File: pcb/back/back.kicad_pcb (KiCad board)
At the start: 4 copper layers, 26.5 x 26.5 mm, 60 parts, among them J1 Conn_01x02, J2 USB_B_Micro, U1 ATSAMD21G18A-A, U2 LSM6DS3, U3 XC6206PxxxMR, U4 TP4057

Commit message: Update accelerometer
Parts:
- U2: value LSM6DS3 -> LIS3DH; footprint Package_LGA:LGA-14_3x2.5mm_P0.5mm_LayoutBorder3x4y -> Package_LGA:LGA-16_3x3mm_P0.5mm_LayoutBorder3x5y
- moved R19 0.15 mm to (159.0, 91.5), turned to -90 degrees
- moved R18 0.14 mm to (159.0, 89.6)
- moved C5 0.13 mm to (154.0, 89.9)
- moved C6 0.13 mm to (154.0, 90.9)
- turned U2 to 90 degrees
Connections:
- U2 pad 1: GND -> +3V3
- U2 pad 10: unconnected-(U2-NC-Pad10) -> GND
- U2 pad 11: unconnected-(U2-NC-Pad11) -> /AINT
- U2 pad 12: +3V3 -> GND
- U2 pad 13: /SCL -> unconnected-(U2-ADC3-Pad13)
- U2 pad 14: /SDA -> +3V3
- U2 pad 4: /AINT -> /SCL
- U2 pad 5: +3V3 -> GND
- U2 pad 6: GND -> /SDA
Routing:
- net /SWDIO: track 19.5 -> 16.0 mm
- net GND: track 10.4 -> 13.4 mm, vias 29 -> 30
- net +3V3: track 62.5 -> 63.9 mm
- net /AINT: track 11.1 -> 11.7 mm

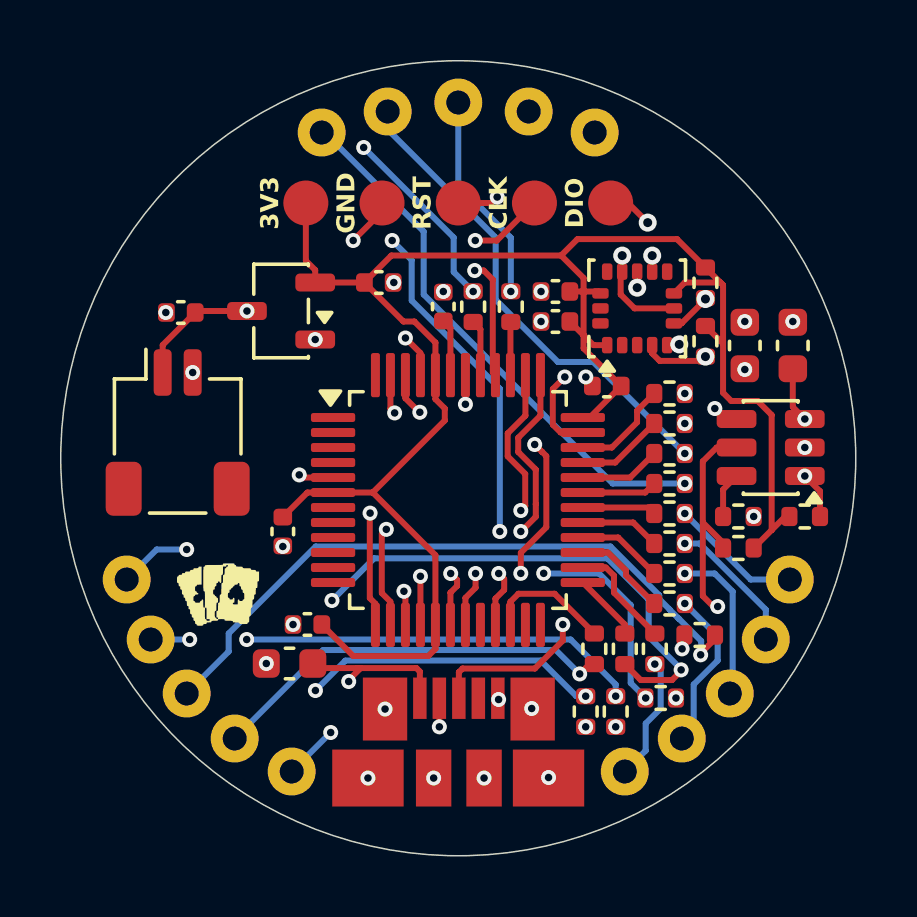
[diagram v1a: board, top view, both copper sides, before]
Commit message: Add tooling holes
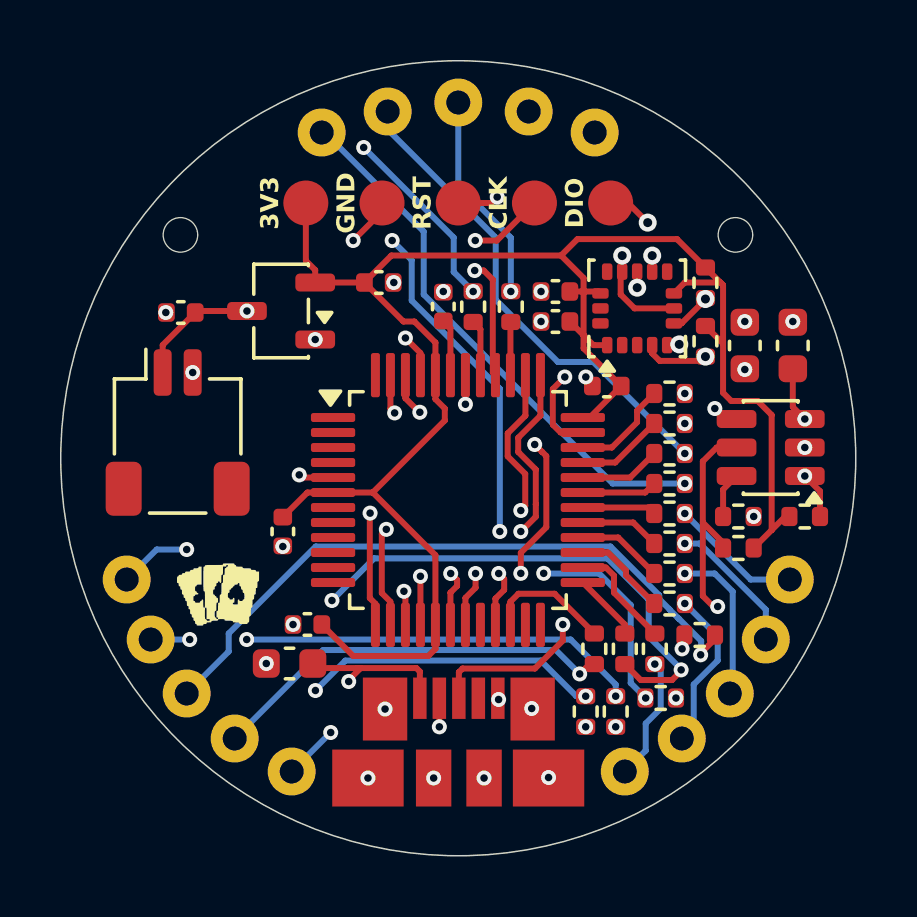
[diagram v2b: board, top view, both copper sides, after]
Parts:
- added REF**: ToolingHole_1.152mm, MountingHole:ToolingHole_1.152mm, F.Cu at (160.0, 88.0)
- added REF**: ToolingHole_1.152mm, MountingHole:ToolingHole_1.152mm, F.Cu at (141.5, 88.0)

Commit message: Format schematics
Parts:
- turned C10 to 0 degrees
- turned C11 to 0 degrees
- turned C3 to 90 degrees
- turned C4 to 90 degrees
- turned C6 to 0 degrees
- turned C8 to 90 degrees
- turned R21 to 180 degrees
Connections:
- C10 pad 1: +3V3 -> GND
- C10 pad 2: GND -> +3V3
- C11 pad 1: VBUS -> GND
- C11 pad 2: GND -> VBUS
- C3 pad 1: GND -> VBUS
- C3 pad 2: VBUS -> GND
- C4 pad 1: GND -> +BATT
- C4 pad 2: +BATT -> GND
- C6 pad 1: +3V3 -> GND
- C6 pad 2: GND -> +3V3
- C8 pad 1: GND -> Net-(U1-VDDCORE)
- C8 pad 2: Net-(U1-VDDCORE) -> GND
- R21 pad 1: Net-(U4-PROG) -> GND
- R21 pad 2: GND -> Net-(U4-PROG)

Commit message: Use 2k I2C resistors
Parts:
- R18, R19: value 10k -> 2k
- turned R18 to 90 degrees
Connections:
- R18 pad 1: +3V3 -> /SDA
- R18 pad 2: /SDA -> +3V3
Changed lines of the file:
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@@
 			)
 		)
-		(property "Value" "10k"
+		(property "Value" "2k"
 			(at 0 1.17 90)
 			(layer "F.Fab")
@@
 	(footprint "Resistor_SMD:R_0402_1005Metric"
 		(layer "F.Cu")
-		(at 159 89.5975 -90)
+		(at 159 89.5975 90)
 		(descr "Resistor SMD 0402 (1005 Metric), square (rectangular) end terminal, IPC-7351 nominal, (Body size source: IPC-SM-782 page 72, https://www.pcb-3d.com/wordpress/wp-content/uploads/ipc-sm-782a_amendment_1_and_2.pdf), generated with kicad-footprint-generator")
 		(tags "resistor")
@@
 			)
 		)
-		(property "Value" "10k"
+		(property "Value" "2k"
 			(at 0 1.17 90)
 			(layer "F.Fab")
@@
 		(duplicate_pad_numbers_are_jumpers no)
 		(fp_line
+			(start -0.153641 -0.38)
+			(end 0.153641 -0.38)
+			(stroke
+				(width 0.12)
+				(type solid)
+			)
+			(layer "F.SilkS")
+		)
+		(fp_line
 			(start -0.153641 0.38)
 			(end 0.153641 0.38)
@@
 		)
 		(fp_line
-			(start -0.153641 -0.38)
-			(end 0.153641 -0.38)
-			(stroke
-				(width 0.12)
-				(type solid)
-			)
-			(layer "F.SilkS")
+			(start 0.93 -0.47)
+			(end 0.93 0.47)
+			(stroke
+				(width 0.05)
+				(type solid)
+			)
+			(layer "F.CrtYd")
+		)
+		(fp_line
+			(start -0.93 -0.47)
+			(end 0.93 -0.47)
+			(stroke
+				(width 0.05)
+				(type solid)
+			)
+			(layer "F.CrtYd")
+		)
+		(fp_line
+			(start 0.93 0.47)
+			(end -0.93 0.47)
+			(stroke
+				(width 0.05)
+				(type solid)
+			)
+			(layer "F.CrtYd")
 		)
 		(fp_line
@@
 		)
 		(fp_line
-			(start 0.93 0.47)
-			(end -0.93 0.47)
-			(stroke
-				(width 0.05)
-				(type solid)
-			)
-			(layer "F.CrtYd")
-		)
-		(fp_line
-			(start -0.93 -0.47)
-			(end 0.93 -0.47)
-			(stroke
-				(width 0.05)
-				(type solid)
-			)
-			(layer "F.CrtYd")
-		)
-		(fp_line
-			(start 0.93 -0.47)
-			(end 0.93 0.47)
-			(stroke
-				(width 0.05)
-				(type solid)
-			)
-			(layer "F.CrtYd")
+			(start 0.525 -0.27)
+			(end 0.525 0.27)
+			(stroke
+				(width 0.1)
+				(type solid)
+			)
+			(layer "F.Fab")
+		)
+		(fp_line
+			(start -0.525 -0.27)
+			(end 0.525 -0.27)
+			(stroke
+				(width 0.1)
+				(type solid)
+			)
+			(layer "F.Fab")
+		)
+		(fp_line
+			(start 0.525 0.27)
+			(end -0.525 0.27)
+			(stroke
+				(width 0.1)
+				(type solid)
+			)
+			(layer "F.Fab")
 		)
 		(fp_line
@@
 			(layer "F.Fab")
 		)
-		(fp_line
-			(start 0.525 0.27)
-			(end -0.525 0.27)
-			(stroke
-				(width 0.1)
-				(type solid)
-			)
-			(layer "F.Fab")
-		)
-		(fp_line
-			(start -0.525 -0.27)
-			(end 0.525 -0.27)
-			(stroke
-				(width 0.1)
-				(type solid)
-			)
-			(layer "F.Fab")
-		)
-		(fp_line
-			(start 0.525 -0.27)
-			(end 0.525 0.27)
-			(stroke
-				(width 0.1)
-				(type solid)
-			)
-			(layer "F.Fab")
-		)
 		(fp_text user "${REFERENCE}"
 			(at 0 0 90)
@@
 		)
 		(pad "1" smd roundrect
-			(at -0.51 0 270)
+			(at -0.51 0 90)
+			(size 0.54 0.64)
+			(layers "F.Cu" "F.Mask" "F.Paste")
+			(roundrect_rratio 0.25)
+			(net "/SDA")
+			(pintype "passive")
+		)
+		(pad "2" smd roundrect
+			(at 0.51 0 90)
 			(size 0.54 0.64)
 			(layers "F.Cu" "F.Mask" "F.Paste")
@@
 			(pintype "passive")
 		)
-		(pad "2" smd roundrect
-			(at 0.51 0 270)
-			(size 0.54 0.64)
-			(layers "F.Cu" "F.Mask" "F.Paste")
-			(roundrect_rratio 0.25)
-			(net "/SDA")
-			(pintype "passive")
-		)

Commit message: Update LED resistors
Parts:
- R1, R10, R11, R12, R13, R14, R15, R2, R3, R4, R5, R6, R7, R8, R9: value 75 -> 120
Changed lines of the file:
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@@
 			)
 		)
-		(property "Value" "75"
+		(property "Value" "120"
 			(at 0 1.17 90)
 			(layer "F.Fab")
@@
 			)
 		)
-		(property "Value" "75"
+		(property "Value" "120"
 			(at 0 1.17 0)
 			(layer "F.Fab")
@@
 			)
 		)
-		(property "Value" "75"
+		(property "Value" "120"
 			(at 0 1.17 90)
 			(layer "F.Fab")
@@
 			)
 		)
-		(property "Value" "75"
+		(property "Value" "120"
 			(at 1.11 2 90)
 			(layer "F.Fab")
@@
 			)
 		)
-		(property "Value" "75"
+		(property "Value" "120"
 			(at 0 1.17 0)
 			(layer "F.Fab")
@@
 			)
 		)
-		(property "Value" "75"
+		(property "Value" "120"
 			(at 0 1.17 90)
 			(layer "F.Fab")
@@
 			)
 		)
-		(property "Value" "75"
+		(property "Value" "120"
 			(at 0 1.17 90)
 			(layer "F.Fab")
@@
 			)
 		)
-		(property "Value" "75"
+		(property "Value" "120"
 			(at 0 1.17 90)
 			(layer "F.Fab")
@@
 			)
 		)
-		(property "Value" "75"
+		(property "Value" "120"
 			(at 0 1.17 0)
 			(layer "F.Fab")
@@
 			)
 		)
-		(property "Value" "75"
+		(property "Value" "120"
 			(at 0 1.17 0)
 			(layer "F.Fab")
@@
 			)
 		)
-		(property "Value" "75"
+		(property "Value" "120"
 			(at 0 1.17 90)
 			(layer "F.Fab")
@@
 			)
 		)
-		(property "Value" "75"
+		(property "Value" "120"
 			(at 0 1.17 0)
 			(layer "F.Fab")
@@
 			)
 		)
-		(property "Value" "75"
+		(property "Value" "120"
 			(at 0 1.17 0)
 			(layer "F.Fab")
@@
 			)
 		)
-		(property "Value" "75"
+		(property "Value" "120"
 			(at 0 1.17 0)
 			(layer "F.Fab")
@@
 			)
 		)
-		(property "Value" "75"
+		(property "Value" "120"
 			(at 0 1.17 90)
 			(layer "F.Fab")
